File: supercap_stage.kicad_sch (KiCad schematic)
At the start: 15 parts, among them Q13 FMMT617, U2 LM321A-TR

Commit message: Add missing part codes
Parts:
- C14: LCSC (none) -> C15849
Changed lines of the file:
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@@
 			)
 		)
-		(property "LCSC" ""
+		(property "LCSC" "C15849"
 			(at 119.38 67.31 0)
 			(effects

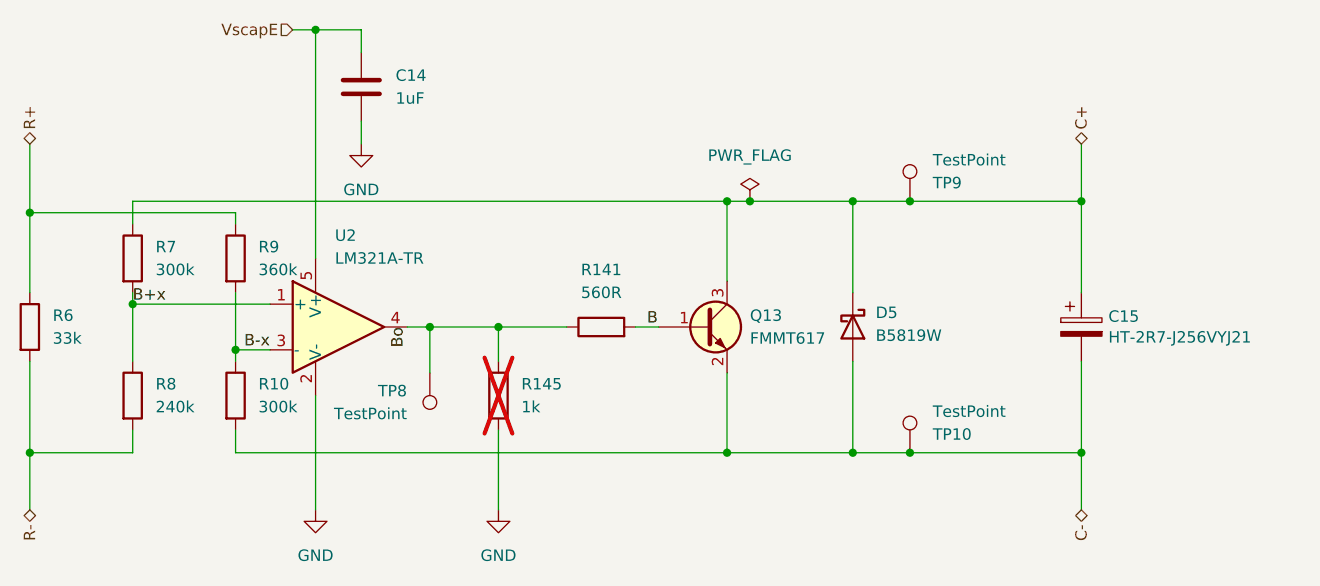
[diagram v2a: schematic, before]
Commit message: Reimplement supercap balancer with a single 4-unit op amp IC
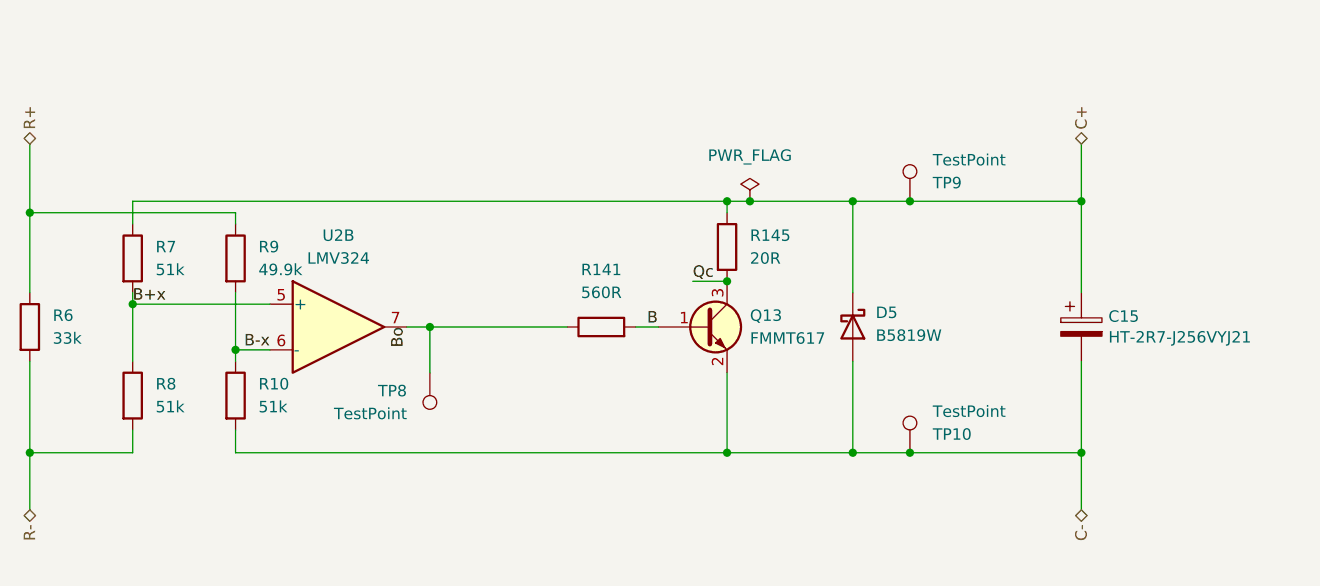
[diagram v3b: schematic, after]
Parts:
- removed C14: 1uF, Capacitor_SMD:C_0603_1608Metric, symbol Device:C
- removed U2: LM321A-TR, Package_TO_SOT_SMD:SOT-23-5, symbol Amplifier_Operational:LM321
- added U2: LMV324, Package_SO:SOIC-14_3.9x8.7mm_P1.27mm, symbol Amplifier_Operational:LMV324
- R10, R7: value 300k -> 51k; footprint Resistor_SMD:R_0603_1608Metric -> Resistor_SMD:R_0402_1005Metric; LCSC C23024 -> (none)
- R141: footprint Resistor_SMD:R_0603_1608Metric -> Resistor_SMD:R_0402_1005Metric; LCSC C23204 -> (none)
- R145: value 1k -> 20R; footprint Resistor_SMD:R_0603_1608Metric -> Resistor_SMD:R_1210_3225Metric; LCSC C21190 -> (none); now fitted
- R8: value 240k -> 51k; footprint Resistor_SMD:R_0603_1608Metric -> Resistor_SMD:R_0402_1005Metric; LCSC C4197 -> (none)
- R9: value 360k -> 49.9k; footprint Resistor_SMD:R_0603_1608Metric -> Resistor_SMD:R_0402_1005Metric; LCSC C23146 -> (none)
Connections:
- net GND is gone; now on net C+: R145.1
- net B+x: now also U2.5 (+)
- net B-x: now also U2.6 (-)
- net Bo: now also U2.7; no longer R145.2
- net C+: no longer Q13.3 (C)
- new net Qc: Q13.3 (C), R145.2

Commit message: Change FLASH footprint and some components for availability
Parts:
- R10, R7, R8: LCSC (none) -> C25794
- R141: footprint Resistor_SMD:R_0402_1005Metric -> Resistor_SMD:R_0603_1608Metric; LCSC (none) -> C23204
- R145: LCSC (none) -> C44451
- R9: LCSC (none) -> C25897
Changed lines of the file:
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@@
 			)
 		)
-		(property "LCSC" ""
+		(property "LCSC" "C25897"
 			(at 105.41 86.36 0)
 			(effects
@@
 			)
 		)
+		(property "LCSC" "C44451"
+			(at 160.02 85.09 0)
+			(effects
+				(font
+					(size 1.27 1.27)
+				)
+				(hide yes)
+			)
+		)
 		(pin "2"
 		)
@@
 			)
 		)
-		(property "LCSC" ""
+		(property "LCSC" "C25794"
 			(at 105.41 101.6 0)
 			(effects
@@
 			)
 		)
-		(property "Footprint" "Resistor_SMD:R_0402_1005Metric"
+		(property "Footprint" "Resistor_SMD:R_0603_1608Metric"
 			(at 146.05 95.758 90)
 			(effects
@@
 			)
 		)
-		(property "LCSC" ""
+		(property "LCSC" "C23204"
 			(at 146.05 93.98 0)
 			(effects
@@
 			)
 		)
-		(property "LCSC" ""
+		(property "LCSC" "C25794"
 			(at 93.98 86.36 0)
 			(effects
@@
 			)
 		)
-		(property "LCSC" ""
+		(property "LCSC" "C25794"
 			(at 93.98 101.6 0)
 			(effects

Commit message: Fix component part numbers
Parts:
- R145: LCSC C44451 -> C620667
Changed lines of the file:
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@@
 			)
 		)
-		(property "LCSC" "C44451"
+		(property "LCSC" "C620667"
 			(at 160.02 85.09 0)
 			(effects

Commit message: Update JLCPCB corrections
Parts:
- Q13: JLCPCB_CORRECTION (none) -> 0;0;180
- U2: JLCPCB_CORRECTION (none) -> 0;0;270
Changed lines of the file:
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@@
+			)
+		)
+		(property "JLCPCB_CORRECTION" "0;0;180"
+			(at 157.48 93.98 0)
+			(effects
+				(font
+					(size 1.27 1.27)
+				)
+				(hide yes)
 			)
 		)
@@
 			(at 116.84 93.98 0)
 			(effects
+				(font
+					(size 1.27 1.27)
+				)
+				(hide yes)
+			)
+		)
+		(property "JLCPCB_CORRECTION" "0;0;270"
+			(at 116.84 93.98 0)
+			(effects
